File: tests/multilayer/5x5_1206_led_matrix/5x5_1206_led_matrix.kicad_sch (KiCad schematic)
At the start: 41 parts, among them J1 USB_C_Receptacle_PowerOnly_6P, J2 Conn_01x06_Pin, U1 ATmega328P-AU, Y1 Crystal_GND23

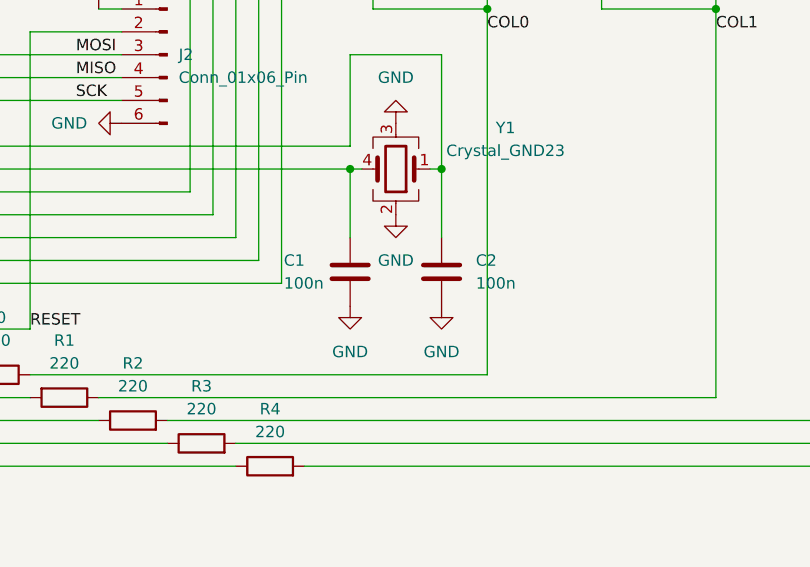
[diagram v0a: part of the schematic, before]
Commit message: test: Correct Value of crystal loading capacitors in 5x5_1206_led_matrix (this is just cosmetic)
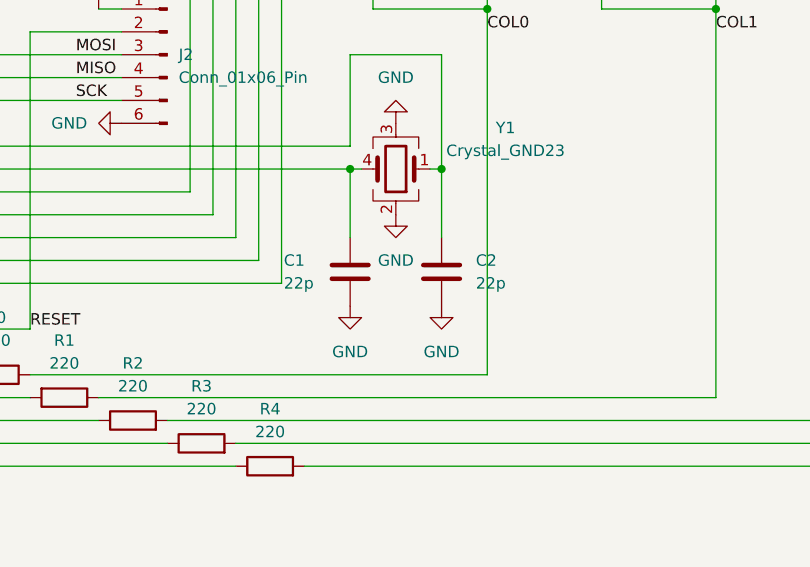
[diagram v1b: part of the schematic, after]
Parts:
- C1, C2: value 100n -> 22p
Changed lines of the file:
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@@
 			)
 		)
-		(property "Value" "100n"
+		(property "Value" "22p"
 			(at 113.03 142.2399 0)
 			(effects
@@
 			)
 		)
-		(property "Value" "100n"
+		(property "Value" "22p"
 			(at 91.694 142.24 0)
 			(effects
